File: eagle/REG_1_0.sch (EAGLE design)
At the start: 12 parts, among them IC1 74HC574N, X1 In A, X2 In B, X3 Out A, X4 Out B, X5 Ctrl

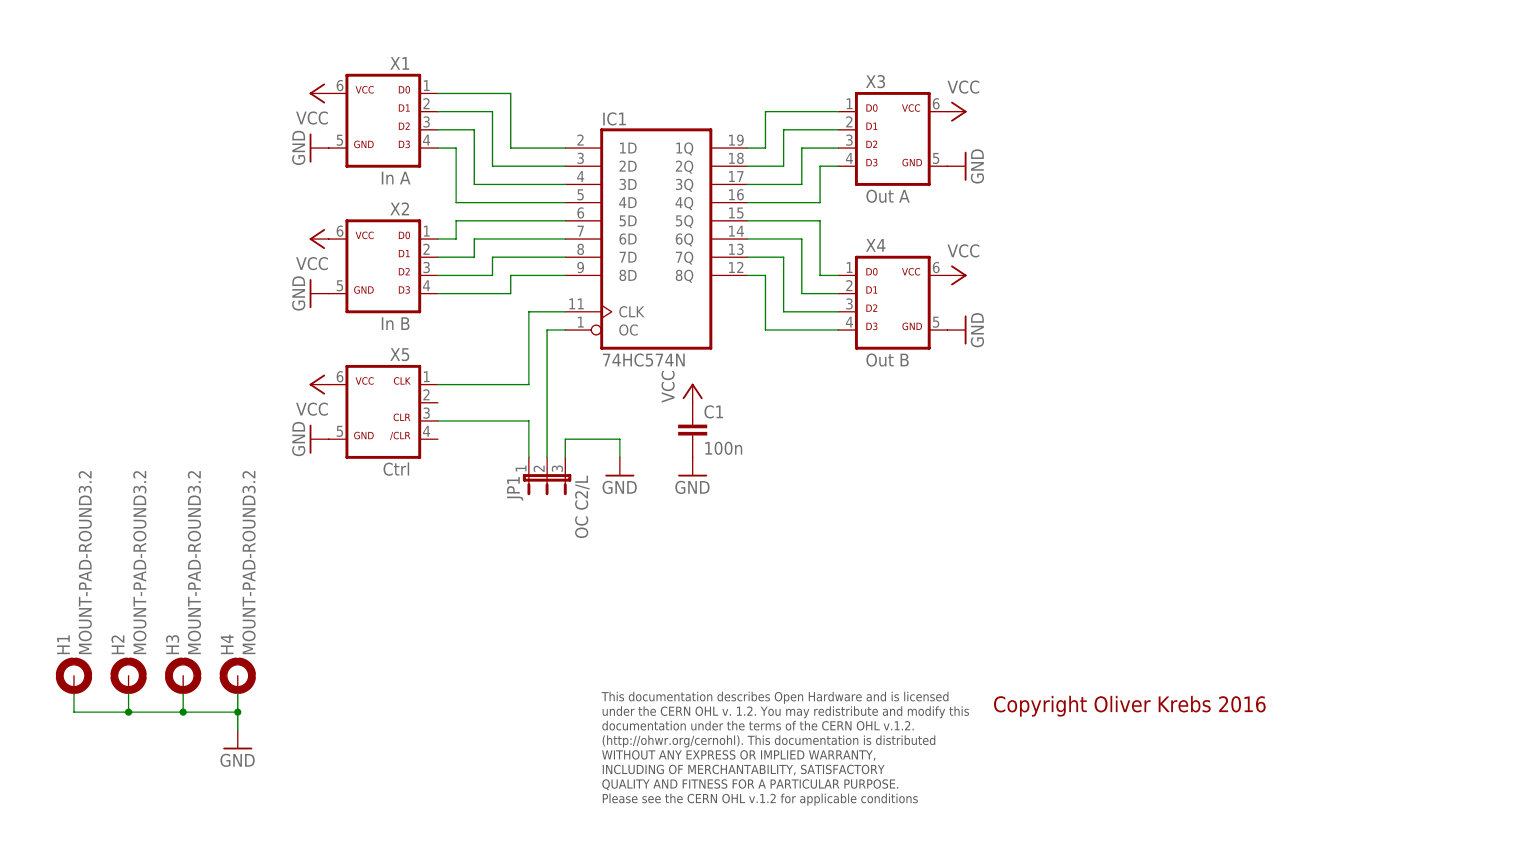
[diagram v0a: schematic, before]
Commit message: Add new tetra-Board and arduino files
Add AMP_1_0, AVC_1_0, D18_1_1, IOP_1_2, MIC_1_0, PIN_1_1, POT_1_0, PWA_1_0, PWR_1_0, RGF 2.0, SOC_2_0, VLT_1_0
Add mex_nano_shield_keyboard, mex_nano_shied_numbers

New arduino projects
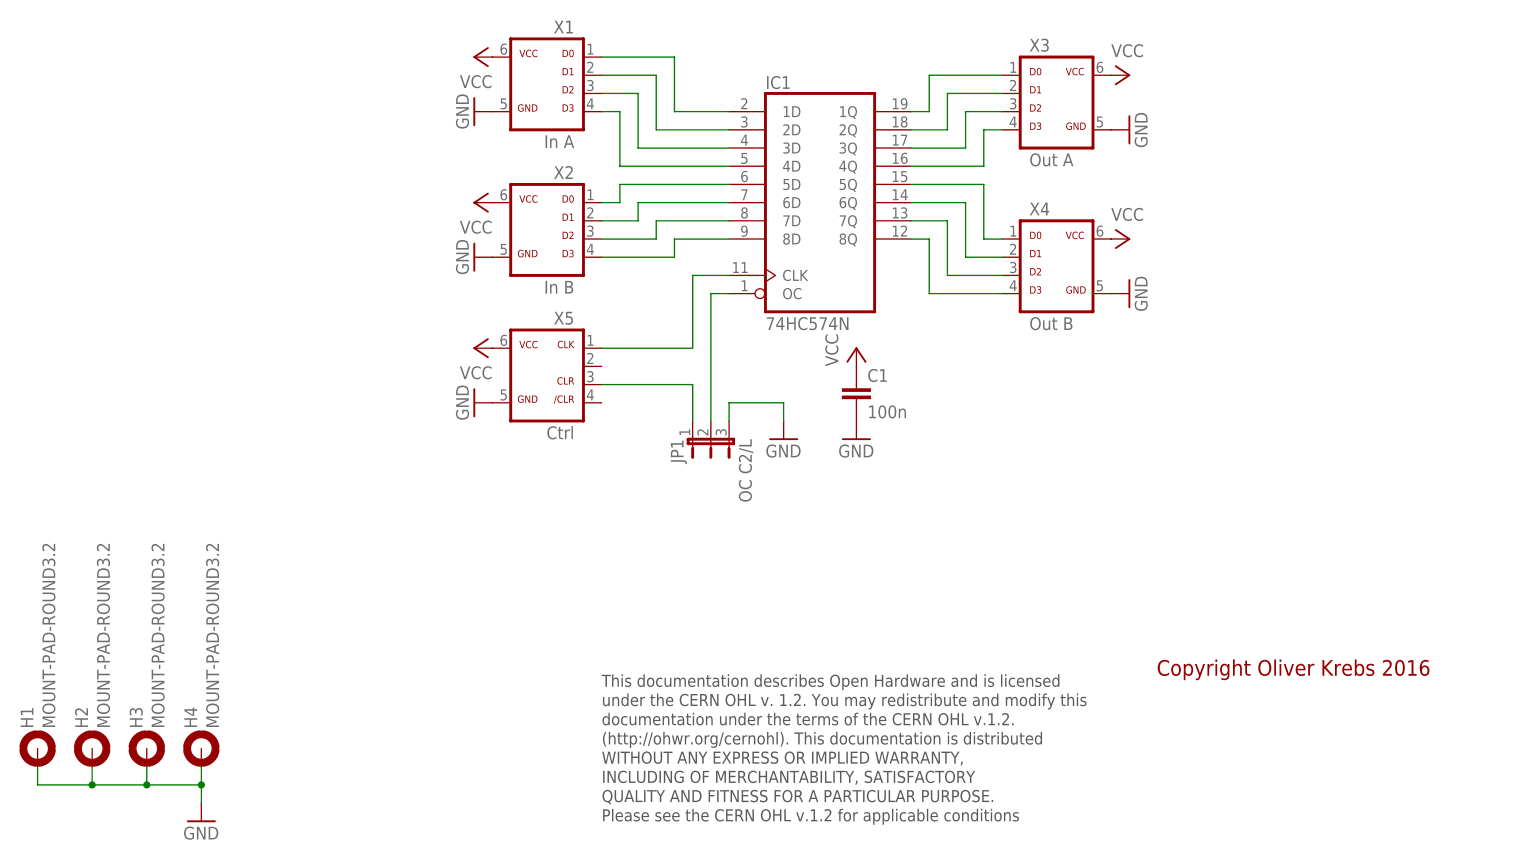
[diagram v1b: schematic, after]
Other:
- moved on the sheet: C1, H1, H2, H3, H4, IC1, JP1, X1, X2, X3, X4, X5
